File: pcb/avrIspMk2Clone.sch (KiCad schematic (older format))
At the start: 41 parts, among them IC1 ATMEGA8-16AU, J1 DB9, P1 USB_OTG, P2 CONN_01X03, P3 CONN_01X02, P4 CONN_02X05, P5 CONN_02X03, SW1 SW_SPDT, U1 LM1117-3.3, Y1 12MHz

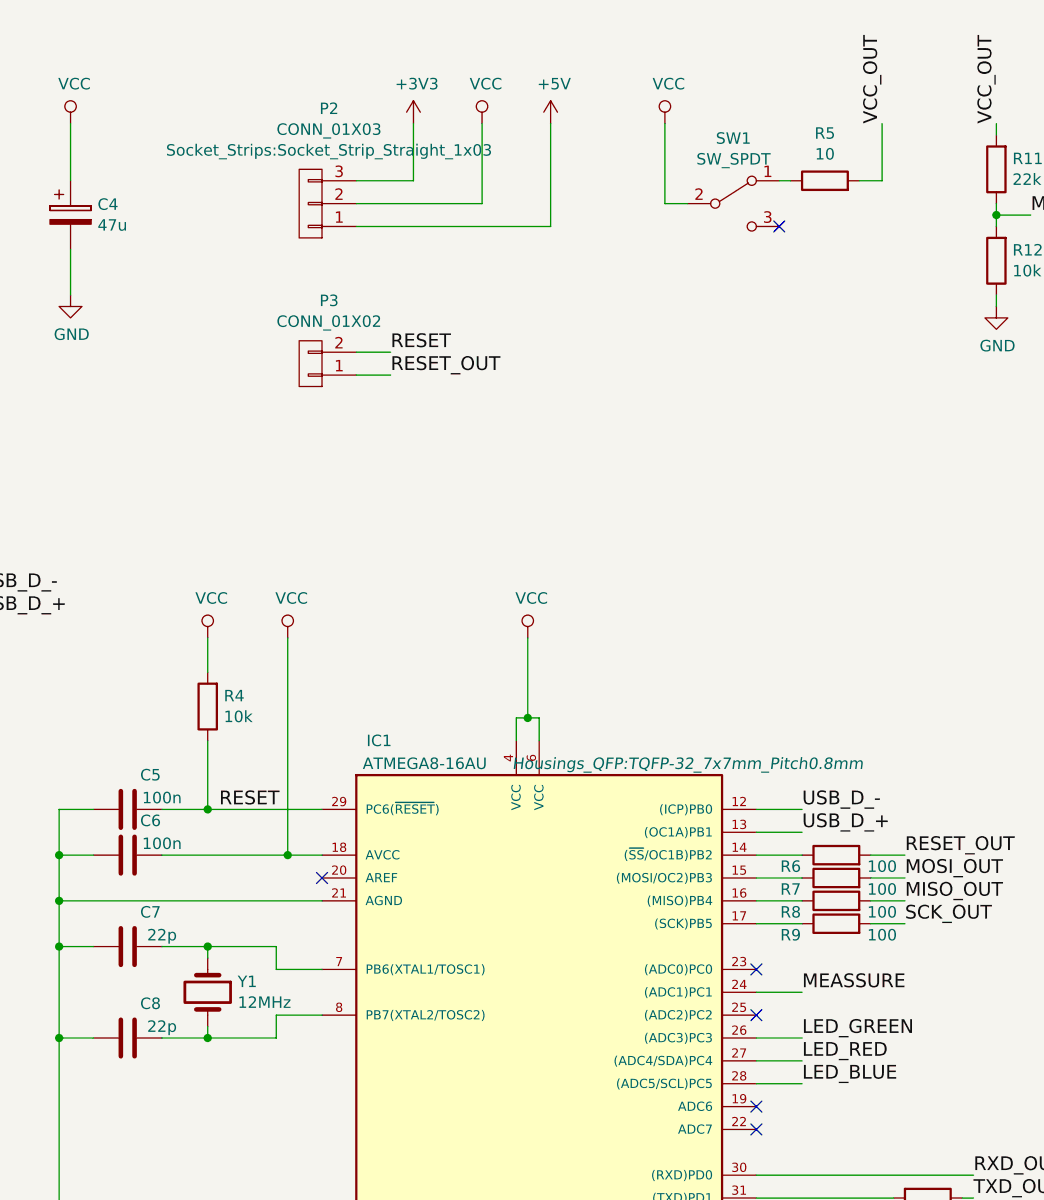
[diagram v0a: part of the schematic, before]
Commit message: Changed the Slide Switch to a Model from Pollin
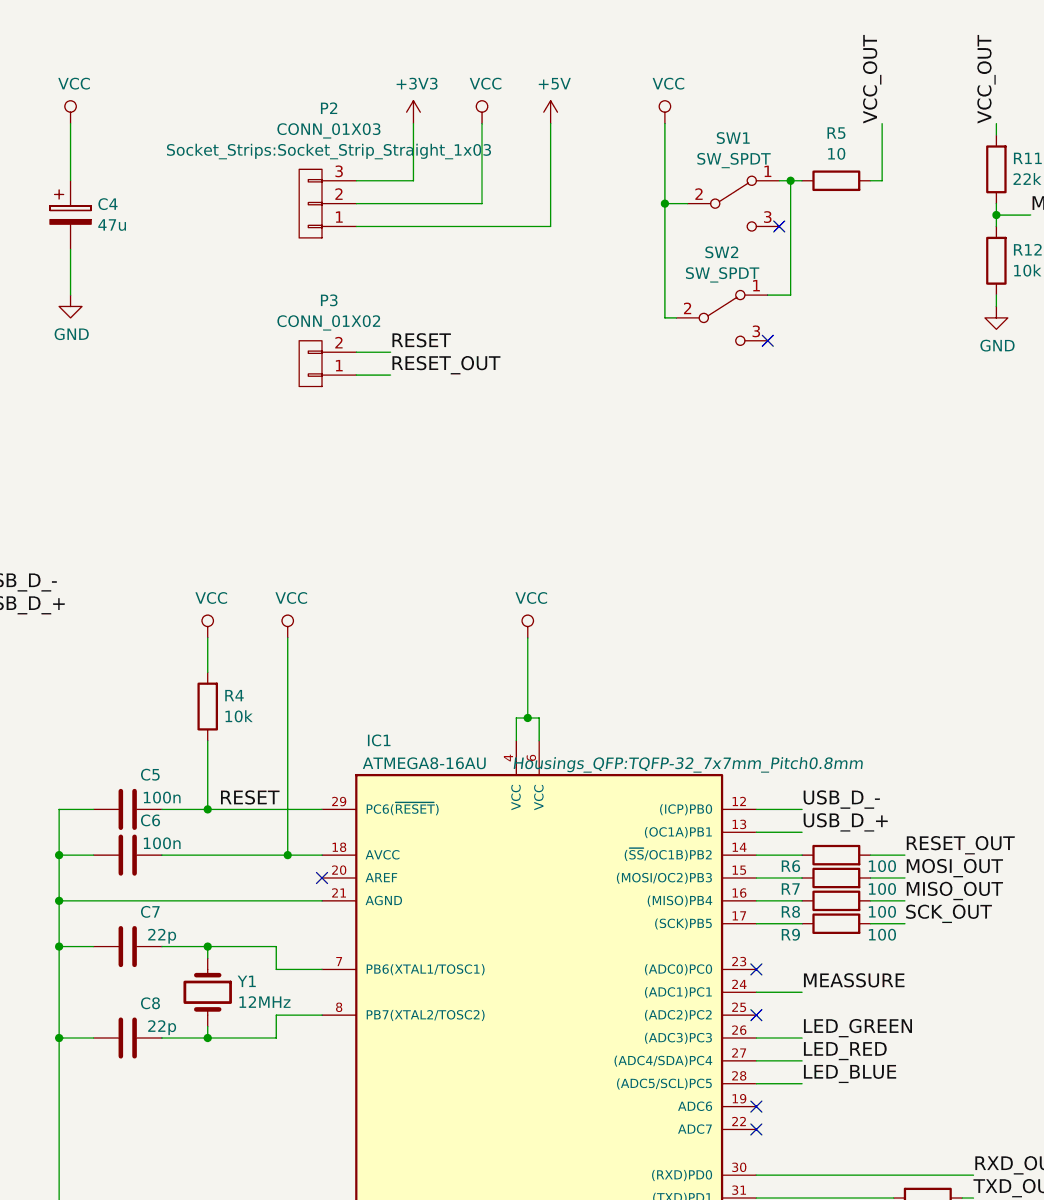
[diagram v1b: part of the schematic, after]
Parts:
- added SW2: SW_SPDT, Pin_Headers:Pin_Header_Straight_1x03_Pitch2.54mm, symbol SW_SPDT
- SW1: footprint Buttons_Switches_THT:SW_Micro_SPST_Angled -> proz_switch:SW_Micro_Slide_3.8
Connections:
- net VCC: now also SW2.2 (B)
- net at R5.1, SW1.1 (A): now also SW2.1 (A)
- no-connect marks 11 -> 12
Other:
- moved on the sheet: R5
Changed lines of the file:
@@
 $EndComp
 $Comp
-L +5V #PWR01
+L +5V #PWR2
 U 1 1 588E56F8
 P 1300 2650
-F 0 "#PWR01" H 1300 2500 50  0001 C CNN
+F 0 "#PWR2" H 1300 2500 50  0001 C CNN
 F 1 "+5V" H 1315 2823 50  0000 C CNN
 F 2 "" H 1300 2650 50  0000 C CNN
@@
 $EndComp
 $Comp
-L +5V #PWR02
+L +5V #PWR5
 U 1 1 588E572F
 P 1850 2650
-F 0 "#PWR02" H 1850 2500 50  0001 C CNN
+F 0 "#PWR5" H 1850 2500 50  0001 C CNN
 F 1 "+5V" H 1865 2823 50  0000 C CNN
 F 2 "" H 1850 2650 50  0000 C CNN
@@
 $EndComp
 $Comp
-L GND #PWR03
+L GND #PWR3
 U 1 1 588E57B0
 P 1300 3900
-F 0 "#PWR03" H 1300 3650 50  0001 C CNN
+F 0 "#PWR3" H 1300 3650 50  0001 C CNN
 F 1 "GND" H 1305 3727 50  0000 C CNN
 F 2 "" H 1300 3900 50  0000 C CNN
@@
 $EndComp
 $Comp
-L GND #PWR04
+L GND #PWR4
 U 1 1 588E57ED
 P 1500 3900
-F 0 "#PWR04" H 1500 3650 50  0001 C CNN
+F 0 "#PWR4" H 1500 3650 50  0001 C CNN
 F 1 "GND" H 1505 3727 50  0000 C CNN
 F 2 "" H 1500 3900 50  0000 C CNN
@@
 $EndComp
 $Comp
-L GND #PWR05
+L GND #PWR6
 U 1 1 588E5810
 P 1850 3900
-F 0 "#PWR05" H 1850 3650 50  0001 C CNN
+F 0 "#PWR6" H 1850 3650 50  0001 C CNN
 F 1 "GND" H 1855 3727 50  0000 C CNN
 F 2 "" H 1850 3900 50  0000 C CNN
@@
 $EndComp
 $Comp
-L +5V #PWR06
+L +5V #PWR1
 U 1 1 588E5997
 P 1150 1150
-F 0 "#PWR06" H 1150 1000 50  0001 C CNN
+F 0 "#PWR1" H 1150 1000 50  0001 C CNN
 F 1 "+5V" H 1165 1323 50  0000 C CNN
 F 2 "" H 1150 1150 50  0000 C CNN
@@
 $EndComp
 $Comp
-L GND #PWR07
+L GND #PWR7
 U 1 1 588E59BA
 P 2000 1900
-F 0 "#PWR07" H 2000 1650 50  0001 C CNN
+F 0 "#PWR7" H 2000 1650 50  0001 C CNN
 F 1 "GND" H 2005 1727 50  0000 C CNN
 F 2 "" H 2000 1900 50  0000 C CNN
@@
 $EndComp
 $Comp
-L +3V3 #PWR08
+L +3V3 #PWR8
 U 1 1 588E5A94
 P 2550 1150
-F 0 "#PWR08" H 2550 1000 50  0001 C CNN
+F 0 "#PWR8" H 2550 1000 50  0001 C CNN
 F 1 "+3V3" H 2565 1323 50  0000 C CNN
 F 2 "" H 2550 1150 50  0000 C CNN
@@
 $EndComp
 $Comp
-L GND #PWR09
+L GND #PWR9
 U 1 1 588E6E52
 P 2950 7050
-F 0 "#PWR09" H 2950 6800 50  0001 C CNN
+F 0 "#PWR9" H 2950 6800 50  0001 C CNN
 F 1 "GND" H 2955 6877 50  0000 C CNN
 F 2 "" H 2950 7050 50  0000 C CNN
@@
 $EndComp
 $Comp
-L VCC #PWR010
+L VCC #PWR14
 U 1 1 588E8343
 P 3600 3400
-F 0 "#PWR010" H 3600 3250 50  0001 C CNN
+F 0 "#PWR14" H 3600 3250 50  0001 C CNN
 F 1 "VCC" H 3617 3573 50  0000 C CNN
 F 2 "" H 3600 3400 50  0000 C CNN
@@
 NoConn ~ 4100 4450
 $Comp
-L VCC #PWR011
+L VCC #PWR15
 U 1 1 588E91A9
 P 3950 3400
-F 0 "#PWR011" H 3950 3250 50  0001 C CNN
+F 0 "#PWR15" H 3950 3250 50  0001 C CNN
 F 1 "VCC" H 3967 3573 50  0000 C CNN
 F 2 "" H 3950 3400 50  0000 C CNN
@@
 	4100 4850 3900 4850
 Wire Wire Line
-	3900 4850 3900 4750
-Wire Wire Line
-	3900 4750 3400 4750
+	3900 4750 3900 4850
+Wire Wire Line
+	3400 4750 3900 4750
 Wire Wire Line
 	3600 4750 3600 4800
@@
 	4100 5050 3900 5050
 Wire Wire Line
-	3900 5050 3900 5150
-Wire Wire Line
-	3900 5150 3400 5150
+	3900 5150 3900 5050
+Wire Wire Line
+	3400 5150 3900 5150
 Wire Wire Line
 	3600 5150 3600 5100
@@
 Connection ~ 2950 4350
 $Comp
-L VCC #PWR012
+L VCC #PWR18
 U 1 1 588E9765
 P 5000 3400
-F 0 "#PWR012" H 5000 3250 50  0001 C CNN
+F 0 "#PWR18" H 5000 3250 50  0001 C CNN
 F 1 "VCC" H 5017 3573 50  0000 C CNN
 F 2 "" H 5000 3400 50  0000 C CNN
@@
 Connection ~ 5000 3750
 $Comp
-L GND #PWR013
+L GND #PWR19
 U 1 1 588E99CC
 P 5000 7050
-F 0 "#PWR013" H 5000 6800 50  0001 C CNN
+F 0 "#PWR19" H 5000 6800 50  0001 C CNN
 F 1 "GND" H 5005 6877 50  0000 C CNN
 F 2 "" H 5000 7050 50  0000 C CNN
@@
 NoConn ~ 6000 4850
 $Comp
-L GND #PWR014
+L GND #PWR28
 U 1 1 588ECEF1
 P 10150 3600
-F 0 "#PWR014" H 10150 3350 50  0001 C CNN
+F 0 "#PWR28" H 10150 3350 50  0001 C CNN
 F 1 "GND" H 10155 3427 50  0000 C CNN
 F 2 "" H 10150 3600 50  0000 C CNN
@@
 $EndComp
 $Comp
-L VCC #PWR015
+L VCC #PWR17
 U 1 1 588EE122
 P 4800 1150
-F 0 "#PWR015" H 4800 1000 50  0001 C CNN
+F 0 "#PWR17" H 4800 1000 50  0001 C CNN
 F 1 "VCC" H 4817 1323 50  0000 C CNN
 F 2 "" H 4800 1150 50  0000 C CNN
@@
 	4800 1500 4250 1500
 $Comp
-L +3V3 #PWR016
+L +3V3 #PWR16
 U 1 1 588EE21D
 P 4500 1150
-F 0 "#PWR016" H 4500 1000 50  0001 C CNN
+F 0 "#PWR16" H 4500 1000 50  0001 C CNN
 F 1 "+3V3" H 4515 1323 50  0000 C CNN
 F 2 "" H 4500 1150 50  0000 C CNN
@@
 	4500 1400 4250 1400
 $Comp
-L +5V #PWR017
+L +5V #PWR20
 U 1 1 588EE36B
 P 5100 1150
-F 0 "#PWR017" H 5100 1000 50  0001 C CNN
+F 0 "#PWR20" H 5100 1000 50  0001 C CNN
 F 1 "+5V" H 5115 1323 50  0000 C CNN
 F 2 "" H 5100 1150 50  0000 C CNN
@@
 	5100 1600 4250 1600
 $Comp
-L GND #PWR018
+L GND #PWR22
 U 1 1 588EE722
 P 7050 1950
-F 0 "#PWR018" H 7050 1700 50  0001 C CNN
+F 0 "#PWR22" H 7050 1700 50  0001 C CNN
 F 1 "GND" H 7055 1777 50  0000 C CNN
 F 2 "" H 7050 1950 50  0000 C CNN
@@
 VCC_OUT
 $Comp
-L VCC #PWR019
+L VCC #PWR21
 U 1 1 588EFDD8
 P 5600 1150
-F 0 "#PWR019" H 5600 1000 50  0001 C CNN
+F 0 "#PWR21" H 5600 1000 50  0001 C CNN
 F 1 "VCC" H 5617 1323 50  0000 C CNN
 F 2 "" H 5600 1150 50  0000 C CNN
@@
 F 0 "SW1" H 5900 1785 50  0000 C CNN
 F 1 "SW_SPDT" H 5900 1694 50  0000 C CNN
-F 2 "Buttons_Switches_THT:SW_Micro_SPST_Angled" H 5900 1500 50  0001 C CNN
+F 2 "proz_switch:SW_Micro_Slide_3.8" H 5900 1500 50  0001 C CNN
 F 3 "" H 5900 1500 50  0000 C CNN
 	1    5900 1500
@@
 	5700 1500 5600 1500
 Wire Wire Line
-	5600 1500 5600 1150
-Wire Wire Line
-	6450 1400 6550 1400
+	5600 1150 5600 2000
+Wire Wire Line
+	6500 1400 6550 1400
 Wire Wire Line
 	6550 1400 6550 1150
@@
 VCC_OUT
 $Comp
-L GND #PWR020
+L GND #PWR29
 U 1 1 588F55F2
 P 10650 6100
-F 0 "#PWR020" H 10650 5850 50  0001 C CNN
+F 0 "#PWR29" H 10650 5850 50  0001 C CNN
 F 1 "GND" H 10655 5927 50  0000 C CNN
 F 2 "" H 10650 6100 50  0000 C CNN
@@
 MOSI_OUT
 $Comp
-L GND #PWR021
+L GND #PWR24
 U 1 1 588FCD39
 P 9050 3850
-F 0 "#PWR021" H 9050 3600 50  0001 C CNN
+F 0 "#PWR24" H 9050 3600 50  0001 C CNN
 F 1 "GND" H 9055 3677 50  0000 C CNN
 F 2 "" H 9050 3850 50  0000 C CNN
@@
 $EndComp
 $Comp
-L GND #PWR022
+L GND #PWR23
 U 1 1 588FCDB9
 P 9050 2800
-F 0 "#PWR022" H 9050 2550 50  0001 C CNN
+F 0 "#PWR23" H 9050 2550 50  0001 C CNN
 F 1 "GND" H 9055 2627 50  0000 C CNN
 F 2 "" H 9050 2800 50  0000 C CNN
@@
 L R R5
 U 1 1 588FA3F2
-P 6300 1400
-F 0 "R5" V 6507 1400 50  0000 C CNN
-F 1 "10" V 6416 1400 50  0000 C CNN
-F 2 "Resistors_SMD:R_0805_HandSoldering" V 6230 1400 50  0001 C CNN
-F 3 "" H 6300 1400 50  0000 C CNN
-	1    6300 1400
+P 6350 1400
+F 0 "R5" V 6557 1400 50  0000 C CNN
+F 1 "10" V 6466 1400 50  0000 C CNN
+F 2 "Resistors_SMD:R_0805_HandSoldering" V 6280 1400 50  0001 C CNN
+F 3 "" H 6350 1400 50  0000 C CNN
+	1    6350 1400
 	0    -1   -1   0
 $EndComp
@@
 $EndComp
 $Comp
-L VCC #PWR023
+L VCC #PWR12
 U 1 1 588FAA92
 P 3500 6550
-F 0 "#PWR023" H 3500 6400 50  0001 C CNN
+F 0 "#PWR12" H 3500 6400 50  0001 C CNN
 F 1 "VCC" H 3517 6723 50  0000 C CNN
 F 2 "" H 3500 6550 50  0000 C CNN
@@
 	3500 6650 3500 6550
 $Comp
-L GND #PWR024
+L GND #PWR13
 U 1 1 588FB147
 P 3500 7050
-F 0 "#PWR024" H 3500 6800 50  0001 C CNN
+F 0 "#PWR13" H 3500 6800 50  0001 C CNN
 F 1 "GND" H 3505 6877 50  0000 C CNN
 F 2 "" H 3500 7050 50  0000 C CNN
@@
 	3500 7050 3500 6950
 $Comp
-L VCC #PWR025
+L VCC #PWR10
 U 1 1 58964567
 P 3000 1150
-F 0 "#PWR025" H 3000 1000 50  0001 C CNN
+F 0 "#PWR10" H 3000 1000 50  0001 C CNN
 F 1 "VCC" H 3017 1323 50  0000 C CNN
 F 2 "" H 3000 1150 50  0000 C CNN
@@
 	3000 1400 3000 1150
 $Comp
-L GND #PWR026
+L GND #PWR11
 U 1 1 589646CC
 P 3000 1900
-F 0 "#PWR026" H 3000 1650 50  0001 C CNN
+F 0 "#PWR11" H 3000 1650 50  0001 C CNN
 F 1 "GND" H 3005 1727 50  0000 C CNN
 F 2 "" H 3000 1900 50  0000 C CNN
@@
 NoConn ~ 6100 1600
 Wire Wire Line
-	6100 1400 6150 1400
-$Comp
-L +5V #PWR?
+	6100 1400 6200 1400
+$Comp
+L +5V #PWR25
 U 1 1 58968C0E
 P 9050 4900
-F 0 "#PWR?" H 9050 4750 50  0001 C CNN
+F 0 "#PWR25" H 9050 4750 50  0001 C CNN
 F 1 "+5V" H 9065 5073 50  0000 C CNN
 F 2 "" H 9050 4900 50  0000 C CNN
@@
 $EndComp
 $Comp
-L +5V #PWR?
+L +5V #PWR26
 U 1 1 589692FC
 P 9450 4900
-F 0 "#PWR?" H 9450 4750 50  0001 C CNN
+F 0 "#PWR26" H 9450 4750 50  0001 C CNN
 F 1 "+5V" H 9465 5073 50  0000 C CNN
 F 2 "" H 9450 4900 50  0000 C CNN
@@
 $EndComp
 $Comp
-L +5V #PWR?
+L +5V #PWR27
 U 1 1 58969382
 P 9850 4900
-F 0 "#PWR?" H 9850 4750 50  0001 C CNN
+F 0 "#PWR27" H 9850 4750 50  0001 C CNN
 F 1 "+5V" H 9865 5073 50  0000 C CNN
 F 2 "" H 9850 4900 50  0000 C CNN
@@
 	1    0    0    -1
 $EndComp
+$Comp
+L SW_SPDT SW2
+U 1 1 58A0CB53
+P 5850 2000
+F 0 "SW2" H 5850 2285 50  0000 C CNN
+F 1 "SW_SPDT" H 5850 2194 50  0000 C CNN
+F 2 "Pin_Headers:Pin_Header_Straight_1x03_Pitch2.54mm" H 5850 2000 50  0001 C CNN
+F 3 "" H 5850 2000 50  0000 C CNN
+	1    5850 2000
+	1    0    0    -1
+$EndComp
+Wire Wire Line
+	5600 2000 5650 2000
+Connection ~ 5600 1500
+NoConn ~ 6050 2100
+Wire Wire Line
+	6050 1900 6150 1900
+Wire Wire Line
+	6150 1900 6150 1400
+Connection ~ 6150 1400
 $EndSCHEMATC

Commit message: changed resistors and caps from 0805 to 0603
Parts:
- C2, C3, C5, C6, C7, C8, C9: footprint Capacitors_SMD:C_0805_HandSoldering -> Capacitors_SMD:C_0603_HandSoldering
- P2: footprint Socket_Strips:Socket_Strip_Straight_1x03 -> Pin_Headers:Pin_Header_Straight_1x03_Pitch2.54mm
- P3: footprint Socket_Strips:Socket_Strip_Straight_1x02 -> Pin_Headers:Pin_Header_Straight_1x02_Pitch2.54mm
- R1, R10, R11, R12, R13, R14, R15, R16, R2, R3, R4, R6, R7, R8, R9: footprint Resistors_SMD:R_0805_HandSoldering -> Resistors_SMD:R_0603_HandSoldering
- R5: value 10 -> 1; footprint Resistors_SMD:R_0805_HandSoldering -> Resistors_SMD:R_0603_HandSoldering
